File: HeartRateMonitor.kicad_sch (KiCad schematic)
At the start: 30 parts, among them J1 USB_C_Receptacle_USB2.0, J2 SWD, J3 Conn_01x08_Pin, U1 CH340E, U2 LMH6702MF, U3 TLV62130, U4 STM32G030F6Px

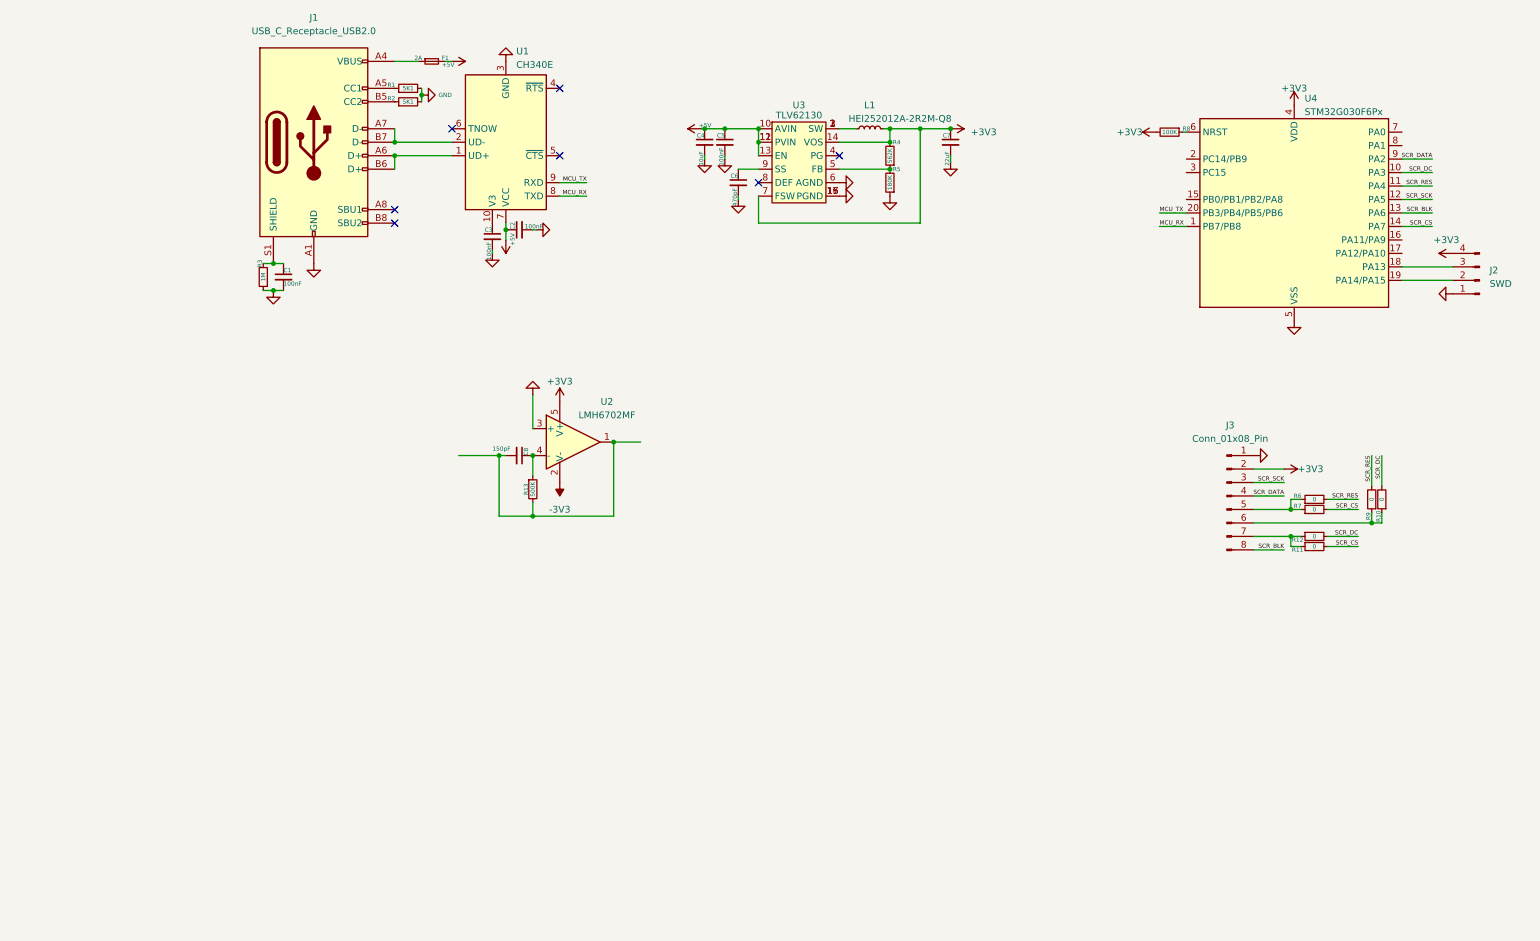
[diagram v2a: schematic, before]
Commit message: low and high pass filter
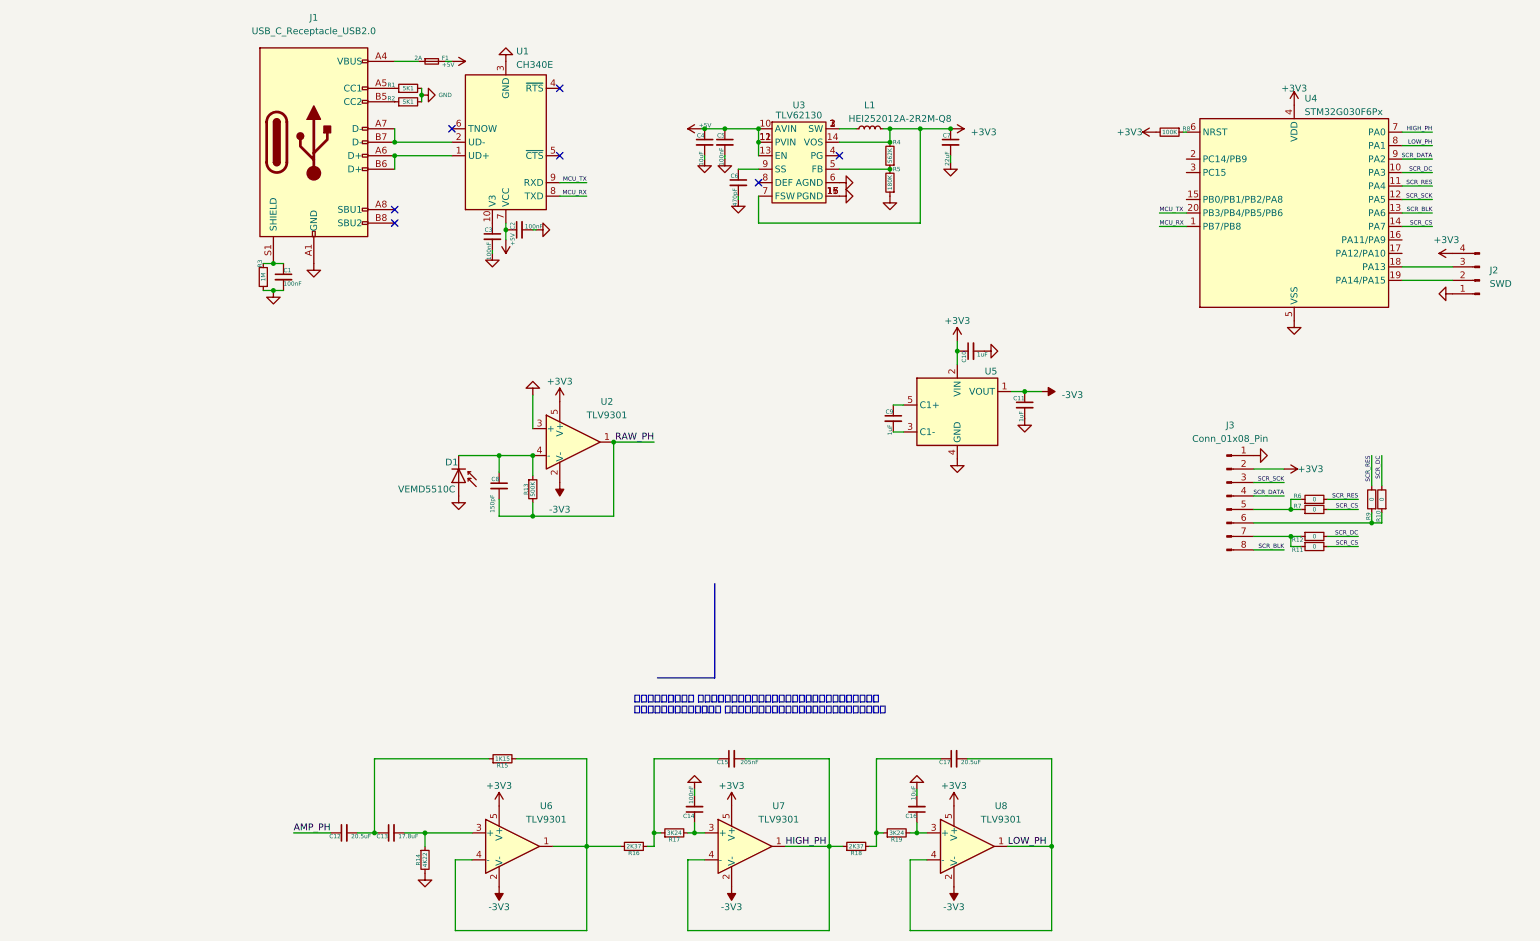
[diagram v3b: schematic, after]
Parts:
- added C10, C11, C9: 1uF, Capacitor_SMD:C_0603_1608Metric, symbol Device:C_Small
- added C12, C17: 20.5uF, Capacitor_SMD:C_0603_1608Metric, symbol Device:C_Small
- added C13: 17.8uF, Capacitor_SMD:C_0603_1608Metric, symbol Device:C_Small
- added C14: 100nF, Capacitor_SMD:C_0603_1608Metric, symbol Device:C_Small
- added C15: 205nF, Capacitor_SMD:C_0603_1608Metric, symbol Device:C_Small
- added C16: 10uF, Capacitor_SMD:C_0603_1608Metric, symbol Device:C_Small
- added D1: VEMD5510C, symbol Device:D_Photo
- added R14: 4K22, Resistor_SMD:R_0603_1608Metric, symbol Device:R_Small
- added R15: 1K15, Resistor_SMD:R_0603_1608Metric, symbol Device:R_Small
- added R16, R18: 2K37, Resistor_SMD:R_0603_1608Metric, symbol Device:R_Small
- added R17, R19: 3K24, Resistor_SMD:R_0603_1608Metric, symbol Device:R_Small
- added U5: ~, symbol HeartRateMonitor:TPS40403
- added U6, U7, U8: TLV9301, Package_TO_SOT_SMD:SOT-23-5, symbol Amplifier_Operational:LMH6702MF
- U2: value LMH6702MF -> TLV9301
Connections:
- net +3V3: now also C10.1, U5.2 (VIN), U6.5 (V+), U7.5 (V+), U8.5 (V+)
- net -3V3: now also C11.1, U5.1 (VOUT), U6.2 (V-), U7.2 (V-), U8.2 (V-)
- net GND: now also C10.2, C11.2, C14.2, C16.2, D1.2 (A), R14.2, U5.4 (GND)
- net at C8.1, R13.1, U2.4 (-): now also D1.1 (K)
- net RAW_PH: now reaches C8.2, R13.2, U2.1
- net HIGH_PH: now reaches U4.7 (PA0)
- net HIGH_PH: now also C15.2, R18.1, U7.1, U7.4 (-)
- net LOW_PH: now reaches U4.8 (PA1)
- net LOW_PH: now also C17.2, U8.1, U8.4 (-)
- new net: C15.1, R16.2, R17.1
- new net: C17.1, R18.2, R19.1
- new net: C16.1, R19.2, U8.3 (+)
- new net: C14.1, R17.2, U7.3 (+)
- new net: R15.2, R16.1, U6.1, U6.4 (-)
- new net: C13.2, R14.1, U6.3 (+)
- new net: C12.2, C13.1, R15.1
- new net: C9.2, U5.3 (C1-)
- new net: C9.1, U5.5 (C1+)
- new net AMP_PH: C12.1
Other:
- note added: "我把这幅杰作留在这 因为我看了半天怎么想也没想明白为啥要把这个电容放在这里 光电二极管的信号频率不高的 在输入脚串电容不就开路了吗？想要有人帮忙指点一下"
- moved on the sheet: C8

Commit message: answer(((
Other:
- note added: "鉴定为困傻了（"
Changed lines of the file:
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@@
     )
+  )
+  (text "鉴定为困傻了（" (exclude_from_sim no)
+ (at 96.52 151.13 0)
+    (effects (font (size 1.27 1.27)) (justify left bottom))
   )
   (text "我把这幅杰作留在这 因为我看了半天怎么想也没想明白为啥要把这个电容放在这里\n光电二极管的信号频率不高的 在输入脚串电容不就开路了吗？想要有人帮忙指点一下\n" (exclude_from_sim no)

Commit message: PGA
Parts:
- added C18: 10uF, Capacitor_SMD:C_0603_1608Metric, symbol Device:C_Small
- added C19: 100nF, Capacitor_SMD:C_0603_1608Metric, symbol Device:C_Small
- added C20: 1uF, Capacitor_SMD:C_0603_1608Metric, symbol Device:C_Small
- added R20, R21: 10K, Resistor_SMD:R_0603_1608Metric, symbol Device:R_Small
- added R22: 1K, Resistor_SMD:R_0603_1608Metric, symbol Device:R_Small
- added U10: TLV9301, Package_TO_SOT_SMD:SOT-23-5, symbol Amplifier_Operational:LMH6702MF
- added U9: AD5272BCP, Package_CSP:LFCSP-WD-10-1EP_3x3mm_P0.5mm_EP1.64x2.38mm, symbol Potentiometer_Digital:AD5272BCP
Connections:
- net +3V3: now also C18.2, C19.2, R20.2, R21.2, U10.5 (V+), U9.1 (VDD), U9.7 (~{RESET})
- net -3V3: now also U10.2 (V-)
- net AMP_PH: now also U10.1, U9.3 (W)
- net GND: now also C18.1, C19.1, C20.2, R22.1, U9.11 (VSS), U9.4 (VSS), U9.6 (GND)
- net RAW_PH: now also U10.3 (+)
- new net: C20.1, U9.5 (EXT_CAP)
- new net DIGIPOT_A: R22.2, U10.4 (-), U9.2 (A)
- new net DIGIPOT_SCL: R20.1, U9.9 (SCL)
- new net DIGIPOT_SDA: R21.1, U9.8 (SDA)
- no-connect marks 7 -> 8
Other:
- note added: "Vdc must >= 7V"

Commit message: refactor
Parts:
- D1: footprint (none) -> FP:VEMD5510C
- U5: value ~ -> TPS60403; footprint (none) -> Package_TO_SOT_SMD:SOT-23-5
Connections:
- net DIGIPOT_SCL: now also U4.16 (PA11/PA9)
- net DIGIPOT_SDA: now also U4.17 (PA12/PA10)
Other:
- moved on the sheet: J2
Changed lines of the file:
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@@
-    (stroke (width 0) (type default))
-  )
-  (wire (pts (xy 236.22 66.04) (xy 245.745 66.04))
     (stroke (width 0) (type default))
   )
@@
     (stroke (width 0) (type default))
   )
+  (wire (pts (xy 236.22 66.04) (xy 248.285 66.04))
+    (stroke (width 0) (type default))
+  )
   (wire (pts (xy 42.545 156.21) (xy 42.545 170.18))
     (stroke (width 0) (type default))
@@
     (stroke (width 0) (type default))
   )
+  (wire (pts (xy 243.84 60.96) (xy 236.22 60.96))
+    (stroke (width 0) (type default))
+  )
   (wire (pts (xy 204.47 138.43) (xy 204.47 141.605))
     (stroke (width 0) (type default))
@@
     (stroke (width 0) (type default))
   )
+  (wire (pts (xy 236.22 58.42) (xy 243.84 58.42))
+    (stroke (width 0) (type default))
+  )
   (wire (pts (xy 111.125 45.085) (xy 114.935 45.085))
     (stroke (width 0) (type default))
@@
     (stroke (width 0) (type default))
   )
-  (wire (pts (xy 236.22 63.5) (xy 245.745 63.5))
+  (wire (pts (xy 236.22 63.5) (xy 248.285 63.5))
     (stroke (width 0) (type default))
   )
@@
     (effects (font (size 0.8 0.8)) (justify right bottom))
   )
+  (label "DIGIPOT_SCL" (at 243.84 58.42 180) (fields_autoplaced)
+    (effects (font (size 0.8 0.8)) (justify right bottom))
+  )
   (label "RAW_PH" (at 95.25 96.52 180) (fields_autoplaced)
     (effects (font (size 1.27 1.27)) (justify right bottom))
@@
     (effects (font (size 0.8 0.8)) (justify right bottom))
   )
+  (label "DIGIPOT_SDA" (at 243.84 60.96 180) (fields_autoplaced)
+    (effects (font (size 0.8 0.8)) (justify right bottom))
+  )
   (label "SCR_RES" (at 241.935 48.26 180) (fields_autoplaced)
     (effects (font (size 0.8 0.8)) (justify right bottom))
@@
     )
   )
-  (symbol (lib_id "power:+3V3") (at 245.745 60.96 90) (unit 1)
-    (in_bom yes) (on_board yes) (dnp no)
-    (property "Reference" "#PWR021" (at 249.555 60.96 0)
-      (effects (font (size 1.27 1.27)) hide)
-    )
-    (property "Value" "+3V3" (at 247.015 58.42 90)
+  (symbol (lib_id "power:+3V3") (at 248.285 60.96 90) (unit 1)
+    (in_bom yes) (on_board yes) (dnp no)
+    (property "Reference" "#PWR021" (at 252.095 60.96 0)
+      (effects (font (size 1.27 1.27)) hide)
+    )
+    (property "Value" "+3V3" (at 249.555 58.42 90)
       (effects (font (size 1.27 1.27)) (justify left))
     )
-    (property "Footprint" "" (at 245.745 60.96 0)
-      (effects (font (size 1.27 1.27)) hide)
-    )
-    (property "Datasheet" "" (at 245.745 60.96 0)
+    (property "Footprint" "" (at 248.285 60.96 0)
+      (effects (font (size 1.27 1.27)) hide)
+    )
+    (property "Datasheet" "" (at 248.285 60.96 0)
       (effects (font (size 1.27 1.27)) hide)
     )
@@
     )
   )
-  (symbol (lib_id "Connector:Conn_01x04_Pin") (at 250.825 66.04 180) (unit 1)
-    (in_bom yes) (on_board yes) (dnp no) (fields_autoplaced)
-    (property "Reference" "J2" (at 252.73 64.135 0)
+  (symbol (lib_id "Connector:Conn_01x04_Pin") (at 253.365 66.04 180) (unit 1)
+    (in_bom yes) (on_board yes) (dnp no) (fields_autoplaced)
+    (property "Reference" "J2" (at 255.27 64.135 0)
       (effects (font (size 1.27 1.27)) (justify right))
     )
-    (property "Value" "SWD" (at 252.73 66.675 0)
+    (property "Value" "SWD" (at 255.27 66.675 0)
       (effects (font (size 1.27 1.27)) (justify right))
     )
-    (property "Footprint" "Connector_PinHeader_2.54mm:PinHeader_1x04_P2.54mm_Vertical" (at 250.825 66.04 0)
-      (effects (font (size 1.27 1.27)) hide)
-    )
-    (property "Datasheet" "~" (at 250.825 66.04 0)
+    (property "Footprint" "Connector_PinHeader_2.54mm:PinHeader_1x04_P2.54mm_Vertical" (at 253.365 66.04 0)
+      (effects (font (size 1.27 1.27)) hide)
+    )
+    (property "Datasheet" "~" (at 253.365 66.04 0)
       (effects (font (size 1.27 1.27)) hide)
     )
@@
       (effects (font (size 1.27 1.27)) (justify left))
     )
-    (property "Footprint" "" (at 58.42 102.87 0)
+    (property "Footprint" "FP:VEMD5510C" (at 58.42 102.87 0)
       (effects (font (size 1.27 1.27)) hide)
     )
@@
       (effects (font (size 1.27 1.27)))
     )
-    (property "Value" "~" (at 152.4 90.805 0)
+    (property "Value" "TPS60403" (at 152.4 90.805 0)
       (effects (font (size 1.27 1.27)))
     )
-    (property "Footprint" "" (at 152.4 90.805 0)
+    (property "Footprint" "Package_TO_SOT_SMD:SOT-23-5" (at 152.4 90.805 0)
       (effects (font (size 1.27 1.27)) hide)
     )
@@
     )
   )
-  (symbol (lib_id "power:GND") (at 245.745 68.58 270) (unit 1)
-    (in_bom yes) (on_board yes) (dnp no) (fields_autoplaced)
-    (property "Reference" "#PWR020" (at 239.395 68.58 0)
-      (effects (font (size 1.27 1.27)) hide)
-    )
-    (property "Value" "GND" (at 241.3 68.58 0)
-      (effects (font (size 1.27 1.27)) hide)
-    )
-    (property "Footprint" "" (at 245.745 68.58 0)
-      (effects (font (size 1.27 1.27)) hide)
-    )
-    (property "Datasheet" "" (at 245.745 68.58 0)
-      (effects (font (size 1.27 1.27)) hide)
-    )
+  (symbol (lib_id "power:GND") (at 248.285 68.58 270) (unit 1)
+    (in_bom yes) (on_board yes) (dnp no) (fields_autoplaced)
+    (property "Reference" "#PWR020" (at 241.935 68.58 0)
+      (effects (font (size 1.27 1.27)) hide)
+    )
+    (property "Value" "GND" (at 243.84 68.58 0)
+      (effects (font (size 1.27 1.27)) hide)
+    )
+    (property "Footprint" "" (at 248.285 68.58 0)
+      (effects (font (size 1.27 1.27)) hide)
+    )
+    (property "Datasheet" "" (at 248.285 68.58 0)
+      (effects (font (size 1.27 1.27)) hide)
+    )

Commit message: add LED
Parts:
- added D2, D3: VLMTG41S2U1, Capacitor_Tantalum_SMD:CP_EIA-3528-21_Kemet-B, symbol Device:LED_Small
- added R23, R24: 4.7R, Resistor_SMD:R_0603_1608Metric, symbol Device:R_Small
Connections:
- net +3V3: now also R23.2, R24.2
- net at U4.2 (PC14/PB9): now also D2.1 (K)
- net at U4.3 (PC15): now also D3.1 (K)
- new net: D2.2 (A), R23.1
- new net: D3.2 (A), R24.1
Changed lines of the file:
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@@
 (kicad_sch (version 20230409) (generator eeschema)
   (paper "A4")
+  (junction (at 165.1 45.72) (diameter 0) (color 0 0 0 0)
+  )
   (junction (at 201.295 132.08) (diameter 0) (color 0 0 0 0)
   )
@@
     (stroke (width 0) (type default))
   )
+  (wire (pts (xy 165.1 43.18) (xy 165.1 45.72))
+    (stroke (width 0) (type default))
+  )
   (wire (pts (xy 114.935 55.245) (xy 145.415 55.245))
     (stroke (width 0) (type default))
@@
     (stroke (width 0) (type default))
   )
+  (wire (pts (xy 165.735 47.625) (xy 165.1 47.625))
+    (stroke (width 0) (type default))
+  )
   (wire (pts (xy 107.315 156.21) (xy 95.25 156.21))
     (stroke (width 0) (type default))
@@
     (stroke (width 0) (type default))
   )
+  (wire (pts (xy 189.23 47.625) (xy 189.23 45.72))
+    (stroke (width 0) (type default))
+  )
   (wire (pts (xy 215.265 116.205) (xy 217.17 116.205))
     (stroke (width 0) (type default))
@@
     (stroke (width 0) (type default))
   )
+  (wire (pts (xy 181.61 43.18) (xy 195.58 43.18))
+    (stroke (width 0) (type default))
+  )
   (wire (pts (xy 215.265 116.205) (xy 215.265 114.3))
     (stroke (width 0) (type default))
@@
     (stroke (width 0) (type default))
   )
+  (wire (pts (xy 163.83 45.72) (xy 165.1 45.72))
+    (stroke (width 0) (type default))
+  )
   (wire (pts (xy 208.28 111.76) (xy 230.505 111.76))
     (stroke (width 0) (type default))
   )
+  (wire (pts (xy 189.23 45.72) (xy 195.58 45.72))
+    (stroke (width 0) (type default))
+  )
   (wire (pts (xy 149.225 156.21) (xy 137.16 156.21))
     (stroke (width 0) (type default))
@@
     (stroke (width 0) (type default))
   )
+  (wire (pts (xy 170.815 43.18) (xy 176.53 43.18))
+    (stroke (width 0) (type default))
+  )
   (wire (pts (xy 241.935 48.26) (xy 236.22 48.26))
     (stroke (width 0) (type default))
   )
+  (wire (pts (xy 165.1 47.625) (xy 165.1 45.72))
+    (stroke (width 0) (type default))
+  )
   (wire (pts (xy 130.175 37.465) (xy 133.35 37.465))
     (stroke (width 0) (type default))
@@
     (stroke (width 0) (type default))
   )
+  (wire (pts (xy 170.815 47.625) (xy 176.53 47.625))
+    (stroke (width 0) (type default))
+  )
   (wire (pts (xy 143.51 188.595) (xy 170.18 188.595))
     (stroke (width 0) (type default))
@@
     (stroke (width 0) (type default))
   )
+  (wire (pts (xy 181.61 47.625) (xy 189.23 47.625))
+    (stroke (width 0) (type default))
+  )
   (wire (pts (xy 66.04 99.06) (xy 66.04 102.235))
     (stroke (width 0) (type default))
@@
     (stroke (width 0) (type default))
   )
+  (wire (pts (xy 165.1 43.18) (xy 165.735 43.18))
+    (stroke (width 0) (type default))
+  )
   (wire (pts (xy 87.63 96.52) (xy 95.25 96.52))
     (stroke (width 0) (type default))
@@
     )
   )
+  (symbol (lib_id "Device:LED_Small") (at 179.07 43.18 180) (unit 1)
+    (in_bom yes) (on_board yes) (dnp no) (fields_autoplaced)
+    (property "Reference" "D2" (at 179.0065 38.1 0)
+      (effects (font (size 1.27 1.27)))
+    )
+    (property "Value" "VLMTG41S2U1" (at 179.0065 40.64 0)
+      (effects (font (size 1.27 1.27)))
+    )
+    (property "Footprint" "Capacitor_Tantalum_SMD:CP_EIA-3528-21_Kemet-B" (at 179.07 43.18 90)
+      (effects (font (size 1.27 1.27)) hide)
+    )
+    (property "Datasheet" "~" (at 179.07 43.18 90)
+      (effects (font (size 1.27 1.27)) hide)
+    )
+    (pin "1")
+    (pin "2")
+    (instances
+      (project "HeartRateMonitor"
+        (path "/3e6a4c48-106f-4ca3-959b-b6cbb3b5c31c"
+          (reference "D2") (unit 1)
+        )
+      )
+    )
+  )
   (symbol (lib_id "power:+3V3") (at 151.765 165.1 0) (unit 1)
     (in_bom yes) (on_board yes) (dnp no) (fields_autoplaced)
@@
     )
   )
+  (symbol (lib_id "Device:LED_Small") (at 179.07 47.625 0) (mirror y) (unit 1)
+    (in_bom yes) (on_board yes) (dnp no)
+    (property "Reference" "D3" (at 179.0065 52.705 0)
+      (effects (font (size 1.27 1.27)))
+    )
+    (property "Value" "VLMTG41S2U1" (at 179.0065 50.165 0)
+      (effects (font (size 1.27 1.27)))
+    )
+    (property "Footprint" "Capacitor_Tantalum_SMD:CP_EIA-3528-21_Kemet-B" (at 179.07 47.625 90)
+      (effects (font (size 1.27 1.27)) hide)
+    )
+    (property "Datasheet" "~" (at 179.07 47.625 90)
+      (effects (font (size 1.27 1.27)) hide)
+    )
+    (pin "1")
+    (pin "2")
+    (instances
+      (project "HeartRateMonitor"
+        (path "/3e6a4c48-106f-4ca3-959b-b6cbb3b5c31c"
+          (reference "D3") (unit 1)
+        )
+      )
+    )
+  )
   (symbol (lib_id "power:GND") (at 130.175 47.625 90) (unit 1)
     (in_bom yes) (on_board yes) (dnp no) (fields_autoplaced)
@@
     )
   )
+  (symbol (lib_id "Device:R_Small") (at 168.275 43.18 270) (unit 1)
+    (in_bom yes) (on_board yes) (dnp no)
+    (property "Reference" "R23" (at 171.45 42.545 90)
+      (effects (font (size 0.8 0.8)))
+    )
+    (property "Value" "4.7R" (at 168.275 43.18 90)
+      (effects (font (size 0.8 0.8)))
+    )
+    (property "Footprint" "Resistor_SMD:R_0603_1608Metric" (at 168.275 43.18 0)
+      (effects (font (size 1.27 1.27)) hide)
+    )
+    (property "Datasheet" "~" (at 168.275 43.18 0)
+      (effects (font (size 1.27 1.27)) hide)
+    )
+    (pin "1")
+    (pin "2")
+    (instances
+      (project "HeartRateMonitor"
+        (path "/3e6a4c48-106f-4ca3-959b-b6cbb3b5c31c"
+          (reference "R23") (unit 1)
+        )
+      )
+    )
+  )
   (symbol (lib_id "power:-3V3") (at 151.765 180.34 180) (unit 1)
     (in_bom yes) (on_board yes) (dnp no)
@@
     )
   )
+  (symbol (lib_id "Device:R_Small") (at 168.275 47.625 270) (unit 1)
+    (in_bom yes) (on_board yes) (dnp no)
+    (property "Reference" "R24" (at 171.45 46.99 90)
+      (effects (font (size 0.8 0.8)))
+    )
+    (property "Value" "4.7R" (at 168.275 47.625 90)
+      (effects (font (size 0.8 0.8)))
+    )
+    (property "Footprint" "Resistor_SMD:R_0603_1608Metric" (at 168.275 47.625 0)
+      (effects (font (size 1.27 1.27)) hide)
+    )
+    (property "Datasheet" "~" (at 168.275 47.625 0)
+      (effects (font (size 1.27 1.27)) hide)
+    )
+    (pin "1")
+    (pin "2")
+    (instances
+      (project "HeartRateMonitor"
+        (path "/3e6a4c48-106f-4ca3-959b-b6cbb3b5c31c"
+          (reference "R24") (unit 1)
+        )
+      )
+    )
+  )
   (symbol (lib_id "power:+3V3") (at 213.995 101.6 270) (unit 1)
     (in_bom yes) (on_board yes) (dnp no)
@@
         )
       )
+    )
+  )
+  (symbol (lib_id "power:+3V3") (at 163.83 45.72 90) (unit 1)
+    (in_bom yes) (on_board yes) (dnp no)
+    (property "Reference" "#PWR054" (at 167.64 45.72 0)
+      (effects (font (size 1.27 1.27)) hide)
+    )
+    (property "Value" "+3V3" (at 161.29 45.72 90)
+      (effects (font (size 1.27 1.27)) (justify left))
+    )
+    (property "Footprint" "" (at 163.83 45.72 0)
+      (effects (font (size 1.27 1.27)) hide)
+    )
+    (property "Datasheet" "" (at 163.83 45.72 0)
+      (effects (font (size 1.27 1.27)) hide)
+    )
+    (pin "1")
+    (instances
+      (project "HeartRateMonitor"
+        (path "/3e6a4c48-106f-4ca3-959b-b6cbb3b5c31c"
+          (reference "#PWR054") (unit 1)
+        )
+      )
